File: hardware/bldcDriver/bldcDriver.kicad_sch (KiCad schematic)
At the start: 95 parts, among them J1 Conn_01x02, J2 Conn_01x06, J4 Conn_01x03, Q13 PMOS, Q14 S8050, U10 AMS1117, U2 STM32G431RBTx, U3 TPS5430DDA, U5 MPU6500, U6 TLV9062xD, U7 MT3608, U8 TLV9062xD, U9 TLV9062xD, Y2 Crystal_GND2_Small

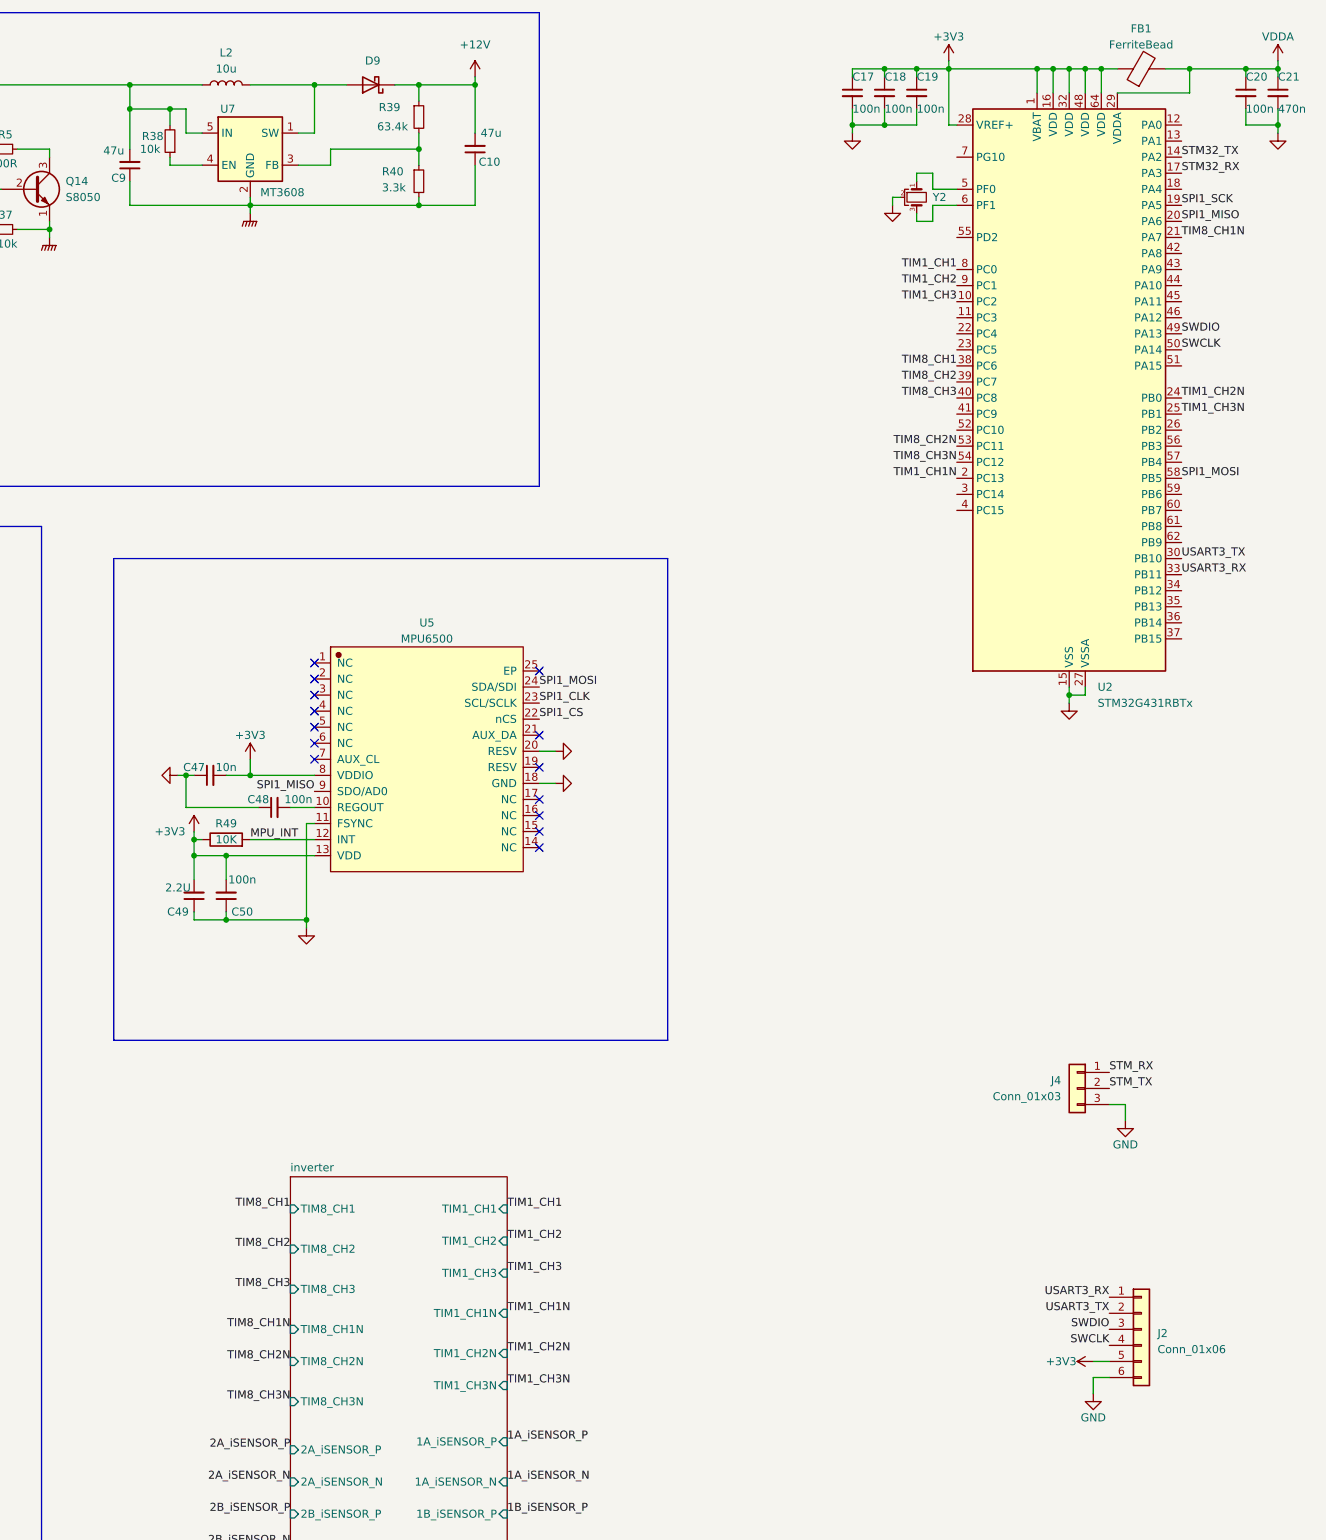
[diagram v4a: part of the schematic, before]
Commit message: update motorDriver sch
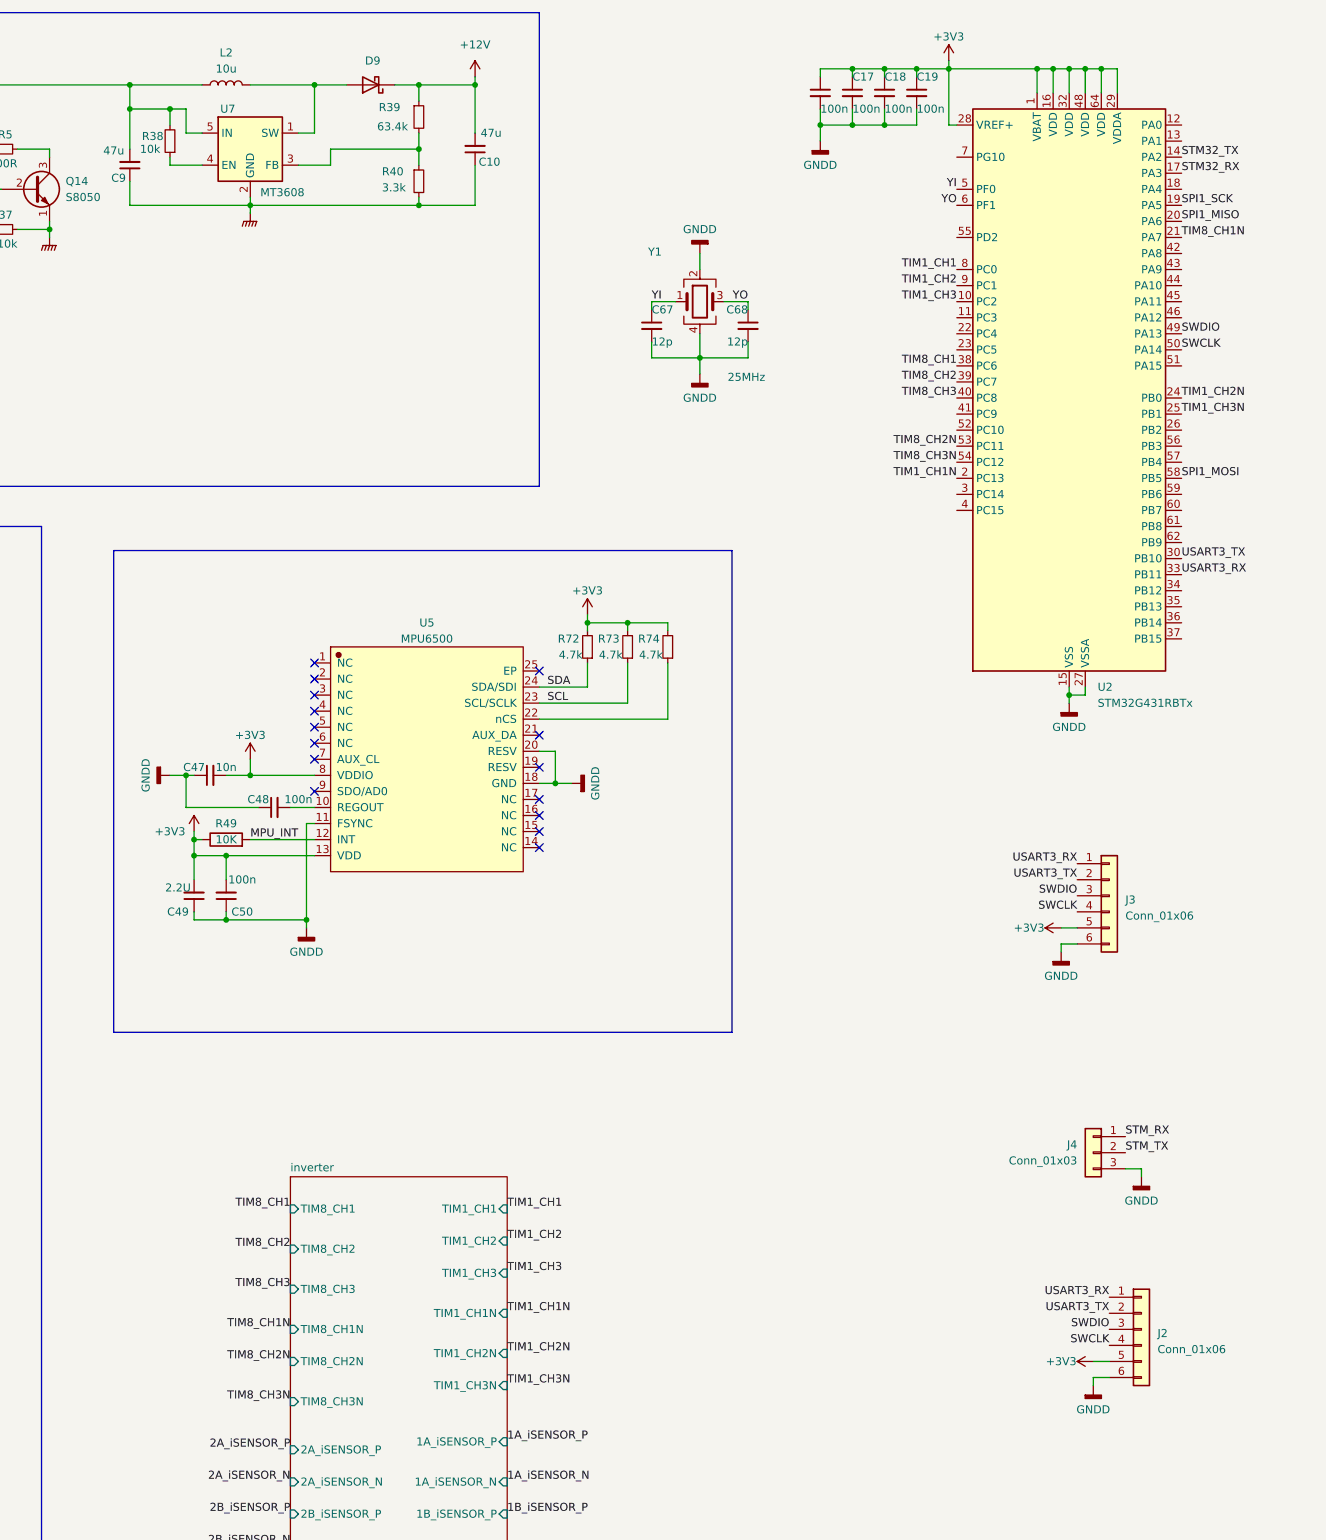
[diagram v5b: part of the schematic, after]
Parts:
- removed C21: 470n, Capacitor_SMD:C_0603_1608Metric_Pad1.08x0.95mm_HandSolder, symbol Device:C_Small
- removed FB1: FerriteBead, Resistor_SMD:R_1206_3216Metric_Pad1.30x1.75mm_HandSolder, symbol Device:FerriteBead
- removed Y2: Crystal_GND2_Small, symbol Device:Crystal_GND2_Small
- added C67, C68: 12p, Capacitor_SMD:C_0603_1608Metric_Pad1.08x0.95mm_HandSolder, symbol Device:C_Small
- added J3: Conn_01x06, balancerDriver:CONN-SMD_BM06B-GHS-TBT-LF-SN, symbol Connector_Generic:Conn_01x06
- added R72, R73, R74: 4.7k, Resistor_SMD:R_0603_1608Metric_Pad0.98x0.95mm_HandSolder, symbol Device:R_Small
- added Y1: 25MHz, Crystal:Crystal_SMD_SeikoEpson_FA238-4Pin_3.2x2.5mm_HandSoldering, symbol Device:Crystal_GND24
- J1: footprint kicadLib:CONN-TH_XT30UPB-M -> balancerDriver:CONN-TH_XT30UPB-M
- J2: footprint kicadLib:CONN-SMD_BM06B-GHS-TBT-LF-SN -> balancerDriver:CONN-SMD_BM06B-GHS-TBT-LF-SN
- J4: footprint kicadLib:CONN-SMD_3P-P1.00_WAFER-SH1.0-3PWB -> balancerDriver:CONN-SMD_3P-P1.00_WAFER-SH1.0-3PWB
- U5: footprint kicadLib:QFN-24_L3.0-W3.0-P0.40-BL-EP -> balancerDriver:QFN-24_L3.0-W3.0-P0.40-BL-EP
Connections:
- net GND is gone; now on net GNDD: C17.2, C18.2, C19.2, C20.2, C47.1, C48.1, C49.1, C50.1, J2.6 (Pin_6), J4.3 (Pin_3), U2.15 (VSS), U2.27 (VSSA), U2.31 (VSS), U2.47 (VSS), U2.63 (VSS), U5.11 (FSYNC), U5.18 (GND), U5.20 (RESV)
- net VDDA is gone; now on net +3V3: C20.1, U2.29 (VDDA)
- net +3V3: now also J3.5 (Pin_5), R72.2, R73.2, R74.2
- net GNDD: now also C67.2, C68.2, J3.6 (Pin_6), Y1.2, Y1.4
- net SPI1_MISO: no longer U5.9 (SDO/AD0)
- net SPI1_MOSI: no longer U5.24 (SDA/SDI)
- net SWCLK: now also J3.4 (Pin_4)
- net SWDIO: now also J3.3 (Pin_3)
- net USART3_RX: now also J3.1 (Pin_1)
- net USART3_TX: now also J3.2 (Pin_2)
- net YI: now reaches U2.5 (PF0)
- net YI: now also C67.1, Y1.1
- net YO: now reaches U2.6 (PF1)
- net YO: now also C68.1, Y1.3
- net SPI1_CLK renamed SCL
- net SCL: now also R73.1
- net SPI1_CS: no longer names the net of U5.22 (nCS)
- net SPI1_CS: now also R74.1
- new net SDA: R72.1, U5.24 (SDA/SDI)
- no-connect marks 15 -> 16
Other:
- moved on the sheet: J4

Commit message: update driver pcb
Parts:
- added C21: 470n, Capacitor_SMD:C_0603_1608Metric_Pad1.08x0.95mm_HandSolder, symbol Device:C_Small
- added J5: Conn_01x06, balancerDriver:CONN-SMD_BM06B-GHS-TBT-LF-SN, symbol Connector_Generic:Conn_01x06
- C10, C2, C3, C4, C9: footprint Capacitor_SMD:C_0805_2012Metric_Pad1.18x1.45mm_HandSolder -> Capacitor_SMD:C_1206_3216Metric_Pad1.33x1.80mm_HandSolder
- FB2: footprint Capacitor_SMD:C_0603_1608Metric_Pad1.08x0.95mm_HandSolder -> Capacitor_SMD:C_1206_3216Metric_Pad1.33x1.80mm_HandSolder
- J2: footprint balancerDriver:CONN-SMD_BM06B-GHS-TBT-LF-SN -> Connector_PinSocket_2.54mm:PinSocket_1x06_P2.54mm_Vertical
- L1: footprint Capacitor_SMD:C_0805_2012Metric_Pad1.18x1.45mm_HandSolder -> Inductor_SMD:L_Sumida_CDMC6D28_7.25x6.5mm
- L2: footprint Capacitor_SMD:C_0805_2012Metric_Pad1.18x1.45mm_HandSolder -> Inductor_SMD:L_Taiyo-Yuden_MD-4040
- Q14: footprint Package_TO_SOT_THT:TO-18-3 -> Package_TO_SOT_SMD:SOT-23
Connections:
- net +3V3: now also C21.1, J5.5 (Pin_5)
- net GNDD: now also C21.2, J5.6 (Pin_6)
- net SPI1_MISO: now also J3.2 (Pin_2), J5.2 (Pin_2)
- net SPI1_MOSI: now also J3.3 (Pin_3), J5.3 (Pin_3)
- net SPI1_SCK: now also J3.1 (Pin_1), J5.1 (Pin_1)
- net SWCLK: no longer J3.4 (Pin_4)
- net SWDIO: no longer J3.3 (Pin_3)
- net TIM1_CH1N: now also U2.35 (PB13); no longer U2.2 (PC13)
- net USART3_RX: no longer J3.1 (Pin_1)
- net USART3_TX: no longer J3.2 (Pin_2)
- net +BATT: now reaches C5.2, C6.2, C7.2, J1.2 (Pin_2), U3.7 (VIN)
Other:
- moved on the sheet: J3

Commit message: update pcbs
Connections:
- net TIM1_CH1N: now also U2.21 (PA7); no longer U2.35 (PB13)
- net TIM8_CH1N: now also U2.56 (PB3); no longer U2.21 (PA7)
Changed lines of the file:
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@@
+		)
+	)
+	(label "TIM1_CH1N"
+		(at 359.41 53.34 0)
+		(fields_autoplaced yes)
+		(effects
+			(font
+				(size 1.27 1.27)
+			)
+			(justify left bottom)
 		)
 	)
@@
 		)
 	)
-	(label "2B_iSENSOR_N"
+	(label "2B_ISENSOR_N"
 		(at 218.44 260.35 180)
 		(fields_autoplaced yes)
@@
 		)
 	)
-	(label "TIM8_CH1N"
-		(at 359.41 53.34 0)
-		(fields_autoplaced yes)
-		(effects
-			(font
-				(size 1.27 1.27)
-			)
-			(justify left bottom)
-		)
-	)
-	(label "2A_iSENSOR_P"
+	(label "2A_ISENSOR_P"
 		(at 218.44 245.11 180)
 		(fields_autoplaced yes)
@@
 		)
 	)
-	(label "1B_iSENSOR_N"
+	(label "1B_ISENSOR_N"
 		(at 252.73 261.62 0)
 		(fields_autoplaced yes)
@@
 		)
 	)
-	(label "1A_iSENSOR_N"
+	(label "1A_ISENSOR_N"
 		(at 252.73 250.19 0)
 		(fields_autoplaced yes)
@@
 		)
 	)
-	(label "1B_iSENSOR_P"
+	(label "1B_ISENSOR_P"
 		(at 252.73 255.27 0)
 		(fields_autoplaced yes)
@@
 		)
 	)
+	(label "TIM8_CH1N"
+		(at 359.41 86.36 0)
+		(fields_autoplaced yes)
+		(effects
+			(font
+				(size 1.27 1.27)
+			)
+			(justify left bottom)
+		)
+	)
 	(label "VREF_OP1"
 		(at 144.78 119.38 0)
@@
 		)
 	)
-	(label "2B_iSENSOR_P"
+	(label "2B_ISENSOR_P"
 		(at 218.44 255.27 180)
 		(fields_autoplaced yes)
@@
 		)
 	)
-	(label "2A_iSENSOR_N"
+	(label "2A_ISENSOR_N"
 		(at 218.44 250.19 180)
 		(fields_autoplaced yes)
@@
 		)
 	)
-	(label "TIM1_CH1N"
-		(at 359.41 111.76 0)
-		(fields_autoplaced yes)
-		(effects
-			(font
-				(size 1.27 1.27)
-			)
-			(justify left bottom)
-		)
-	)
 	(label "VREF_OP2"
 		(at 97.79 242.57 180)
@@
 		)
 	)
-	(label "1A_iSENSOR_P"
+	(label "1A_ISENSOR_P"
 		(at 252.73 243.84 0)
 		(fields_autoplaced yes)
